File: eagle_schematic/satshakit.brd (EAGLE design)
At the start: 55.4 x 42.5 mm, 16 parts

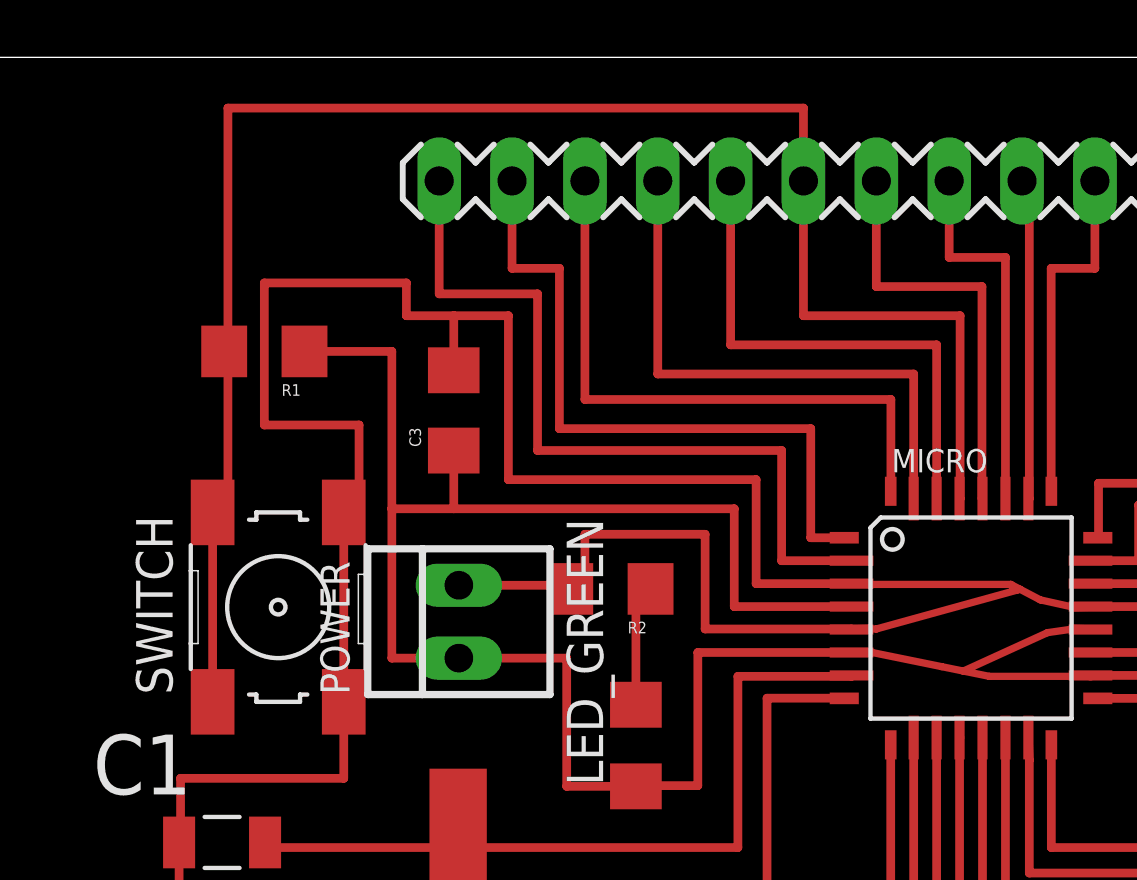
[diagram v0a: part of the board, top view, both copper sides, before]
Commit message: v0.2 programming from FTDI cable
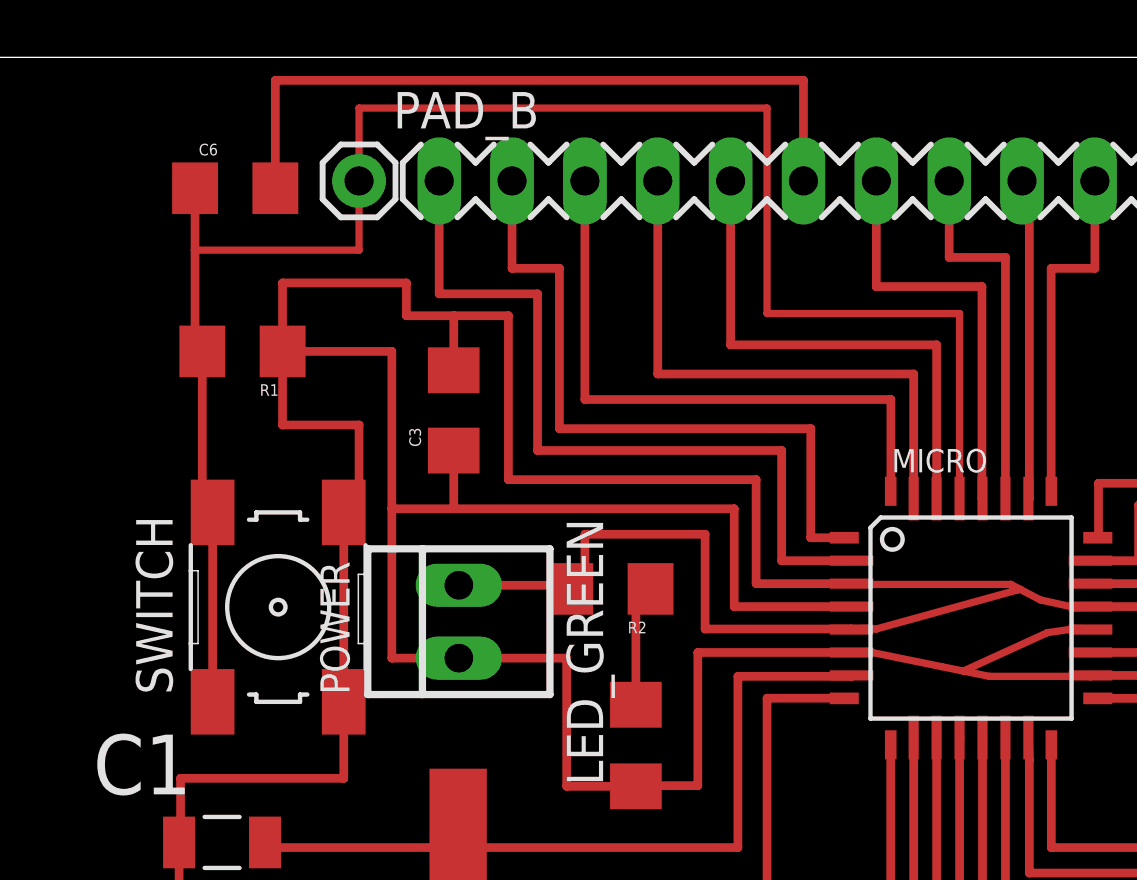
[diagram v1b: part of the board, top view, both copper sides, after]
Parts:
- added C6: 100pF, 01_SparkFun:1206
- added PAD_B: M01PTH, 01_SparkFun:1X01
- moved R1 0.76 mm to (21.6, 29.6)
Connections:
- new net N$28: C6.1, MICRO.29, PAD_B.1, R1.2, SWITCH.1, SWITCH.2
- net N$3: now also C6.2; no longer MICRO.29, R1.2, SWITCH.1, SWITCH.2
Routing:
- net N$28: track 0.00 -> 64.2 mm
- net N$3: track 60.8 -> 25.7 mm
- net GND: track 163.9 -> 162.7 mm
- net VCC: track 87.5 -> 88.2 mm
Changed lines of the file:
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@@
 <attribute name="OC_FARNELL" value="unknown" x="29.1084" y="7.5692" size="1.778" layer="27" rot="R90" display="off"/>
 </element>
-<element name="R1" library="01_SparkFun" package="1206" value="10k" x="22.352" y="29.6164" rot="R180"/>
+<element name="R1" library="01_SparkFun" package="1206" value="10k" x="21.59" y="29.6164" rot="R180"/>
 <element name="SWITCH" library="01_FAB_Hello" package="6MM_SWITCH" value="" x="22.8346" y="20.701" rot="R90"/>
 <element name="POWER" library="con-molex" package="22-23-2021" value="22-23-2021" x="29.1338" y="20.193" rot="R90">
@@
 <element name="C4" library="01_SparkFun" package="1206" value="1uF" x="60.452" y="19.177" rot="R90"/>
 <element name="C5" library="01_SparkFun" package="1206" value="100pF" x="63.754" y="19.177" rot="R90"/>
+<element name="C6" library="01_SparkFun" package="1206" value="100pF" x="21.336" y="35.306"/>
+<element name="PAD_B" library="01_SparkFun" package="1X01" value="M01PTH" x="25.654" y="35.56"/>
 </elements>
 <signals>
@@
 <wire x1="38.735" y1="20.72" x2="38.735" y2="24.13" width="0.3048" layer="1"/>
 <wire x1="38.735" y1="24.13" x2="28.956" y2="24.13" width="0.3048" layer="1"/>
-<wire x1="23.752" y1="29.6164" x2="26.797" y2="29.6164" width="0.3048" layer="1"/>
 <wire x1="26.797" y1="29.6164" x2="26.797" y2="24.13" width="0.3048" layer="1"/>
 <wire x1="26.797" y1="24.13" x2="26.797" y2="18.923" width="0.3048" layer="1"/>
@@
 <wire x1="60.452" y1="17.78" x2="60.452" y2="17.777" width="0" layer="19" extent="1-1"/>
 <wire x1="29.337" y1="26.032" x2="28.956" y2="26.159" width="0" layer="19" extent="1-1"/>
+<wire x1="26.797" y1="29.6164" x2="22.99" y2="29.6164" width="0.3048" layer="1"/>
 </signal>
 <signal name="N$2">
@@
 <wire x1="25.1206" y1="24.003" x2="25.654" y2="23.876" width="0.3048" layer="1"/>
 <wire x1="25.654" y1="23.876" x2="25.654" y2="27.051" width="0.3048" layer="1"/>
-<wire x1="25.654" y1="27.051" x2="22.352" y2="27.051" width="0.3048" layer="1"/>
-<wire x1="22.352" y1="27.051" x2="22.352" y2="32.004" width="0.3048" layer="1"/>
-<wire x1="22.352" y1="32.004" x2="27.305" y2="32.004" width="0.3048" layer="1"/>
 <contactref element="R2" pad="2"/>
 <wire x1="33.525" y1="21.209" x2="33.017" y2="21.336" width="0.3048" layer="1"/>
@@
 <contactref element="C3" pad="2"/>
 <wire x1="28.956" y1="28.959" x2="28.956" y2="30.861" width="0.3048" layer="1"/>
-</signal>
-<signal name="N$3">
-<contactref element="MICRO" pad="29"/>
-<contactref element="R1" pad="2"/>
-<contactref element="SWITCH" pad="2"/>
-<contactref element="SWITCH" pad="1"/>
-<wire x1="20.5486" y1="24.003" x2="20.5486" y2="17.399" width="0.3048" layer="1"/>
-<wire x1="46.59" y1="24.4856" x2="46.612" y2="24.4856" width="0.3048" layer="1"/>
-<wire x1="46.59" y1="24.4856" x2="46.609" y2="24.4856" width="0.3048" layer="1"/>
-<wire x1="46.609" y1="24.4856" x2="46.609" y2="30.861" width="0.3048" layer="1"/>
-<wire x1="46.609" y1="30.861" x2="41.148" y2="30.861" width="0.3048" layer="1"/>
-<wire x1="21.082" y1="38.1" x2="41.148" y2="38.1" width="0.3048" layer="1"/>
-<wire x1="41.148" y1="30.861" x2="41.148" y2="35.56" width="0.3048" layer="1"/>
-<contactref element="PADS_2" pad="9"/>
-<wire x1="41.148" y1="38.1" x2="41.148" y2="35.56" width="0.3048" layer="1"/>
-<wire x1="20.5486" y1="24.003" x2="21.082" y2="23.876" width="0.3048" layer="1"/>
-<wire x1="21.082" y1="23.876" x2="21.082" y2="28.956" width="0.3048" layer="1"/>
-<wire x1="21.082" y1="28.956" x2="20.952" y2="28.956" width="0.3048" layer="1"/>
-<wire x1="20.952" y1="28.956" x2="20.952" y2="29.6164" width="0.3048" layer="1"/>
-<wire x1="20.952" y1="29.6164" x2="21.082" y2="29.6164" width="0.3048" layer="1"/>
-<wire x1="21.082" y1="29.6164" x2="21.082" y2="38.1" width="0.3048" layer="1"/>
+<wire x1="27.305" y1="32.004" x2="22.987" y2="32.004" width="0.3048" layer="1"/>
+<wire x1="22.987" y1="32.004" x2="22.987" y2="27.051" width="0.3048" layer="1"/>
+<wire x1="22.987" y1="27.051" x2="25.654" y2="27.051" width="0.3048" layer="1"/>
 </signal>
 <signal name="N$1">
@@
 <wire x1="65.278" y1="15.367" x2="57.937" y2="15.367" width="0.3048" layer="1"/>
 </signal>
+<signal name="N$28">
+<contactref element="R1" pad="2"/>
+<contactref element="SWITCH" pad="1"/>
+<contactref element="SWITCH" pad="2"/>
+<wire x1="20.5486" y1="17.399" x2="20.447" y2="17.399" width="0.4064" layer="1"/>
+<contactref element="MICRO" pad="29"/>
+<contactref element="C6" pad="1"/>
+<wire x1="25.654" y1="38.1" x2="39.878" y2="38.1" width="0.254" layer="1"/>
+<wire x1="39.878" y1="38.1" x2="39.878" y2="30.9372" width="0.254" layer="1"/>
+<wire x1="39.878" y1="30.9372" x2="46.59" y2="30.9372" width="0.254" layer="1"/>
+<wire x1="46.59" y1="30.9372" x2="46.59" y2="24.4856" width="0.254" layer="1"/>
+<contactref element="PAD_B" pad="1"/>
+<wire x1="20.5486" y1="17.399" x2="20.5486" y2="24.003" width="0.3048" layer="1"/>
+<wire x1="20.5486" y1="24.003" x2="20.952" y2="24.003" width="0.3048" layer="1"/>
+<wire x1="20.5486" y1="24.003" x2="20.19" y2="24.003" width="0.3048" layer="1"/>
+<wire x1="20.19" y1="24.003" x2="20.19" y2="29.6164" width="0.3048" layer="1"/>
+<wire x1="20.19" y1="29.6164" x2="19.936" y2="29.6164" width="0.3048" layer="1"/>
+<wire x1="19.936" y1="29.6164" x2="19.936" y2="33.147" width="0.3048" layer="1"/>
+<wire x1="19.936" y1="33.147" x2="19.936" y2="35.306" width="0.3048" layer="1"/>
+<wire x1="25.654" y1="38.1" x2="25.654" y2="35.56" width="0.254" layer="1"/>
+<wire x1="25.654" y1="35.56" x2="25.654" y2="33.147" width="0.254" layer="1"/>
+<wire x1="25.654" y1="33.147" x2="19.936" y2="33.147" width="0.254" layer="1"/>
+</signal>
+<signal name="N$3">
+<contactref element="PADS_2" pad="9"/>
+<contactref element="C6" pad="2"/>
+<wire x1="22.736" y1="39.0652" x2="41.148" y2="39.0652" width="0.3048" layer="1"/>
+<wire x1="41.148" y1="39.0652" x2="41.148" y2="35.56" width="0.3048" layer="1"/>
+<wire x1="22.736" y1="39.0652" x2="22.736" y2="35.306" width="0.3048" layer="1"/>
+</signal>
 </signals>

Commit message: fixed a little error on the board
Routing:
- net GND: track 162.7 -> 165.4 mm
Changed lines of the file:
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@@
 <contactref element="C3" pad="2"/>
 <wire x1="28.956" y1="28.959" x2="28.956" y2="30.861" width="0.3048" layer="1"/>
-<wire x1="27.305" y1="32.004" x2="22.987" y2="32.004" width="0.3048" layer="1"/>
-<wire x1="22.987" y1="32.004" x2="22.987" y2="27.051" width="0.3048" layer="1"/>
-<wire x1="22.987" y1="27.051" x2="25.654" y2="27.051" width="0.3048" layer="1"/>
+<wire x1="27.305" y1="32.004" x2="21.59" y2="32.004" width="0.3048" layer="1"/>
+<wire x1="21.59" y1="32.004" x2="21.59" y2="27.051" width="0.3048" layer="1"/>
+<wire x1="21.59" y1="27.051" x2="25.654" y2="27.051" width="0.3048" layer="1"/>
 </signal>
 <signal name="N$1">

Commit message: minor fixes
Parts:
- C6: value 100pF -> 100nF
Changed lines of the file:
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@@
 <element name="C4" library="01_SparkFun" package="1206" value="1uF" x="60.452" y="19.177" rot="R90"/>
 <element name="C5" library="01_SparkFun" package="1206" value="100pF" x="63.754" y="19.177" rot="R90"/>
-<element name="C6" library="01_SparkFun" package="1206" value="100pF" x="21.336" y="35.306"/>
+<element name="C6" library="01_SparkFun" package="1206" value="100nF" x="21.336" y="35.306"/>
 <element name="PAD_B" library="01_SparkFun" package="1X01" value="M01PTH" x="25.654" y="35.56"/>
 </elements>

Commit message: minor fixes
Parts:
- C5: value 100pF -> 100nF
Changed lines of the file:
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@@
 <element name="C3" library="01_SparkFun" package="1206" value="10uF" x="28.956" y="27.559" rot="R90"/>
 <element name="C4" library="01_SparkFun" package="1206" value="1uF" x="60.452" y="19.177" rot="R90"/>
-<element name="C5" library="01_SparkFun" package="1206" value="100pF" x="63.754" y="19.177" rot="R90"/>
+<element name="C5" library="01_SparkFun" package="1206" value="100nF" x="63.754" y="19.177" rot="R90"/>
 <element name="C6" library="01_SparkFun" package="1206" value="100nF" x="21.336" y="35.306"/>
 <element name="PAD_B" library="01_SparkFun" package="1X01" value="M01PTH" x="25.654" y="35.56"/>
